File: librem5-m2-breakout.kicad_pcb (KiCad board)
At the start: 4 copper layers, 30 x 22 mm, 16 parts, among them J101 M.2_Key_E, J102 Conn_01x02, J103 Conn_02x03_Counter_Clockwise, J104 Conn_02x03_Counter_Clockwise, J105 Conn_01x01, J106 Conn_01x03, J107 Conn_01x02, J108 USB_B_Micro, J109 Micro_SD, U101 SN74LV1T34DBV

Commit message: Make the USB net class's trace clearance 0.15mm
The DRC violation that was occuring doesn't realize that the global clearance is less than the diff pair spacing.
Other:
- net class USB: clearance 0.157 -> 0.15
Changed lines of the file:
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@@
   )
   (net_class USB ""
-    (clearance 0.157)
+    (clearance 0.15)
     (trace_width 0.246)
     (via_dia 0.8)

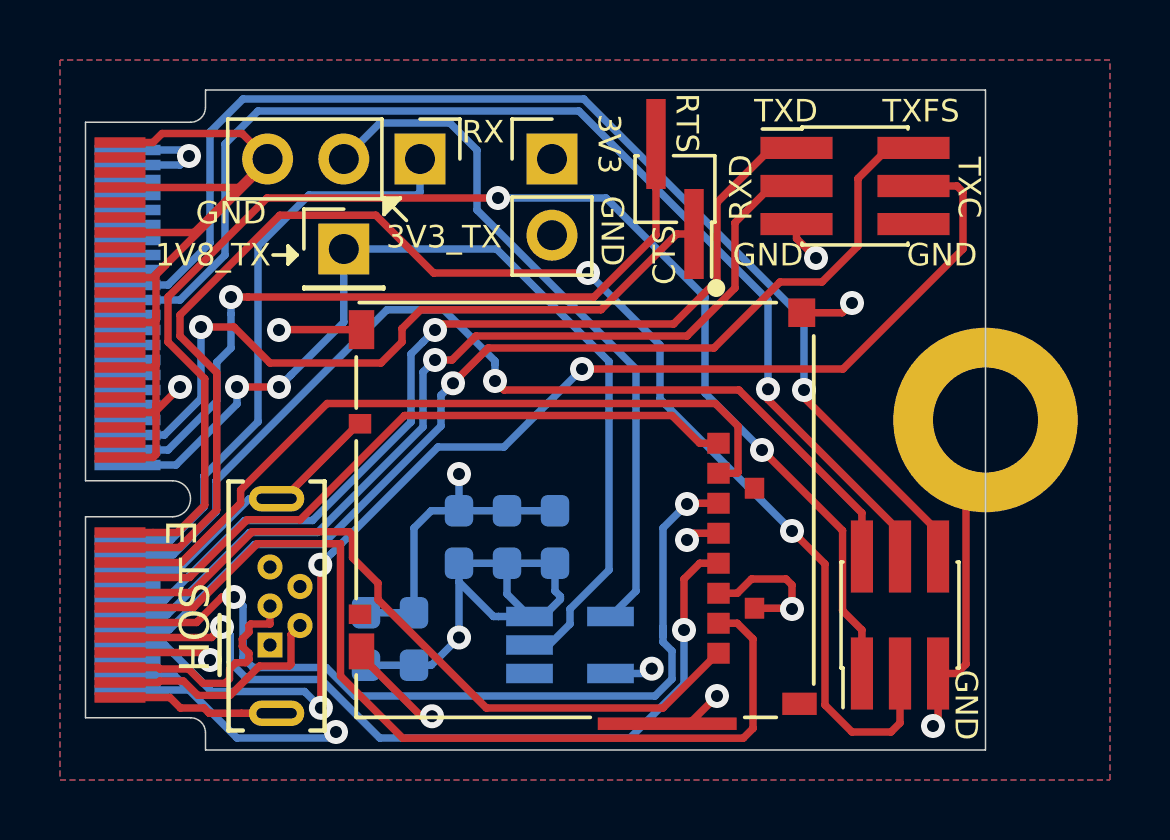
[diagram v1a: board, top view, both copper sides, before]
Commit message: Adjust a couple of traces so they are routed slightly shorted
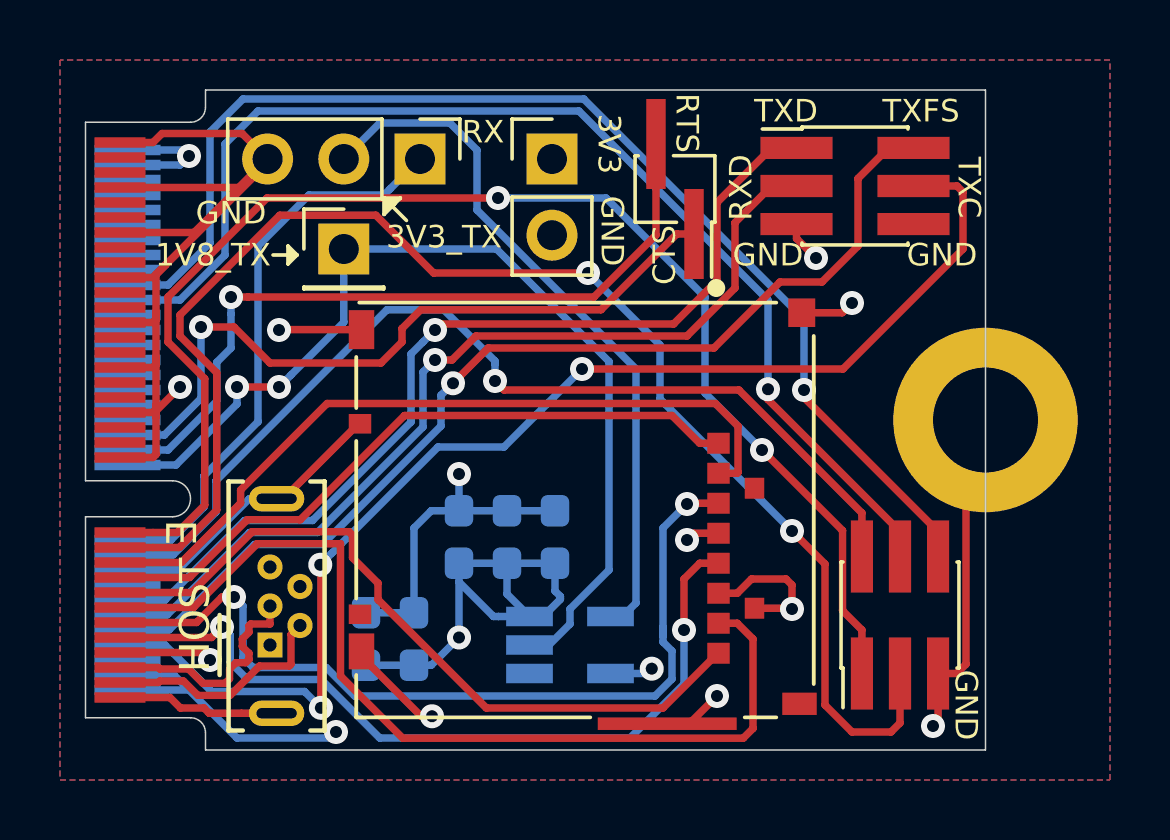
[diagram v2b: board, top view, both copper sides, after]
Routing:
- net /SoC_UART_RX: track 19.7 -> 19.1 mm
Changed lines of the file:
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@@
     (thickness 0.8)
     (drawings 49)
-    (tracks 420)
+    (tracks 421)
     (zones 0)
     (modules 16)
@@
   (segment (start 128.89864 91.324997) (end 130.79067 91.324997) (width 0.25) (layer B.Cu) (net 26))
   (segment (start 123.2 97.023637) (end 128.89864 91.324997) (width 0.25) (layer B.Cu) (net 26))
-  (segment (start 130 87.4) (end 130 86.3) (width 0.25) (layer B.Cu) (net 27))
-  (segment (start 126.3 87.5) (end 129.9 87.5) (width 0.25) (layer B.Cu) (net 27))
-  (segment (start 129.9 87.5) (end 130 87.4) (width 0.25) (layer B.Cu) (net 27))
+  (segment (start 129 87.3) (end 130 86.3) (width 0.25) (layer B.Cu) (net 27))
+  (segment (start 126.3 87.5) (end 128.8 87.5) (width 0.25) (layer B.Cu) (net 27))
+  (segment (start 128.8 87.5) (end 129 87.3) (width 0.25) (layer B.Cu) (net 27))
   (segment (start 124.6 89.2) (end 126.3 87.5) (width 0.25) (layer B.Cu) (net 27))
-  (segment (start 121.7 99) (end 122.8 97.9) (width 0.25) (layer B.Cu) (net 27))
   (segment (start 120.25 99) (end 121.7 99) (width 0.25) (layer B.Cu) (net 27))
   (segment (start 122.8 97.9) (end 122.8 96.857937) (width 0.25) (layer B.Cu) (net 27))
+  (segment (start 121.7 99) (end 122.8 97.9) (width 0.25) (layer B.Cu) (net 27))
   (segment (start 122.8 96.857937) (end 124.6 95.057937) (width 0.25) (layer B.Cu) (net 27))
   (segment (start 124.6 95.057937) (end 124.6 89.2) (width 0.25) (layer B.Cu) (net 27))
@@
   (segment (start 140.600001 96.749999) (end 140.600001 95.204999) (width 0.25) (layer F.Cu) (net 54))
   (segment (start 121.1 99.75) (end 120 99.75) (width 0.25) (layer F.Cu) (net 54))
-  (segment (start 137.2 100.7) (end 136.35 101.55) (width 0.25) (layer B.Cu) (net 55))
+  (segment (start 137.2 93.3) (end 137.2 101.1) (width 0.25) (layer B.Cu) (net 55))
   (segment (start 128.66 85.1) (end 130.995002 85.1) (width 0.25) (layer B.Cu) (net 55))
-  (segment (start 137.2 93.3) (end 137.2 100.7) (width 0.25) (layer B.Cu) (net 55))
   (segment (start 127.46 86.3) (end 128.66 85.1) (width 0.25) (layer B.Cu) (net 55))
+  (segment (start 136.75 101.55) (end 136.35 101.55) (width 0.25) (layer B.Cu) (net 55))
   (segment (start 131.9 86.004998) (end 131.9 88) (width 0.25) (layer B.Cu) (net 55))
   (segment (start 130.995002 85.1) (end 131.9 86.004998) (width 0.25) (layer B.Cu) (net 55))
+  (segment (start 137.2 101.1) (end 136.75 101.55) (width 0.25) (layer B.Cu) (net 55))
   (segment (start 131.9 88) (end 137.2 93.3) (width 0.25) (layer B.Cu) (net 55))
   (zone (net 0) (net_name "") (layer F.Mask) (hatch edge 0.508)
